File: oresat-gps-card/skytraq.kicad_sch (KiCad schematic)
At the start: 12 parts, among them U23 ORION-B16

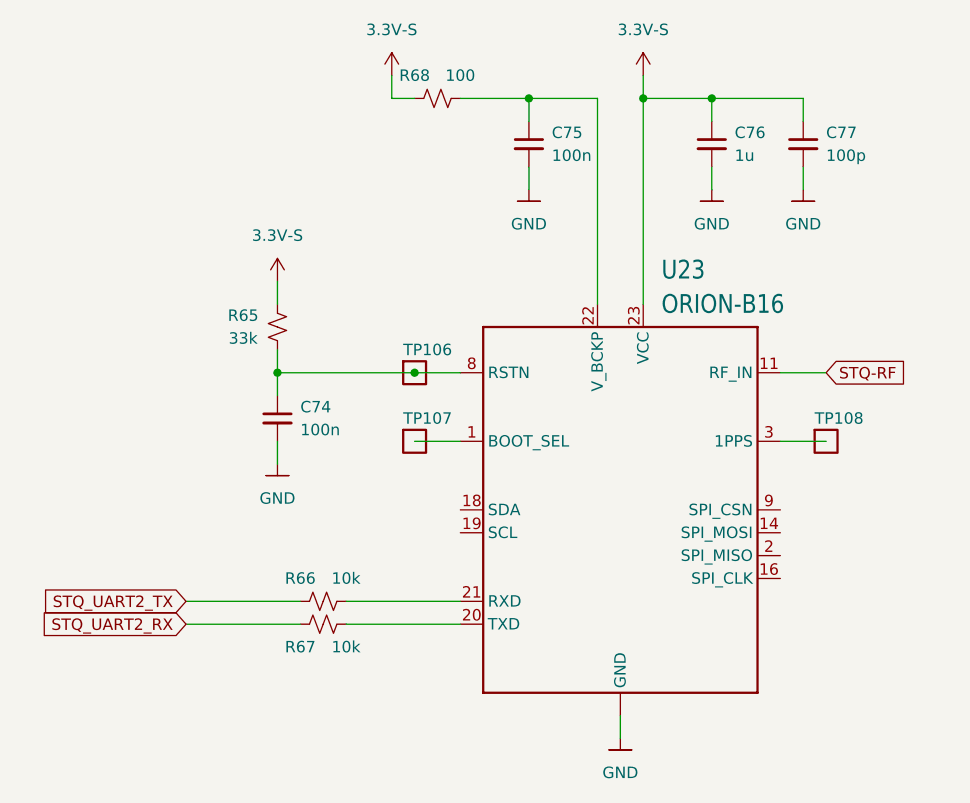
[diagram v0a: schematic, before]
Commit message: GPS card design review changes and issue fixes
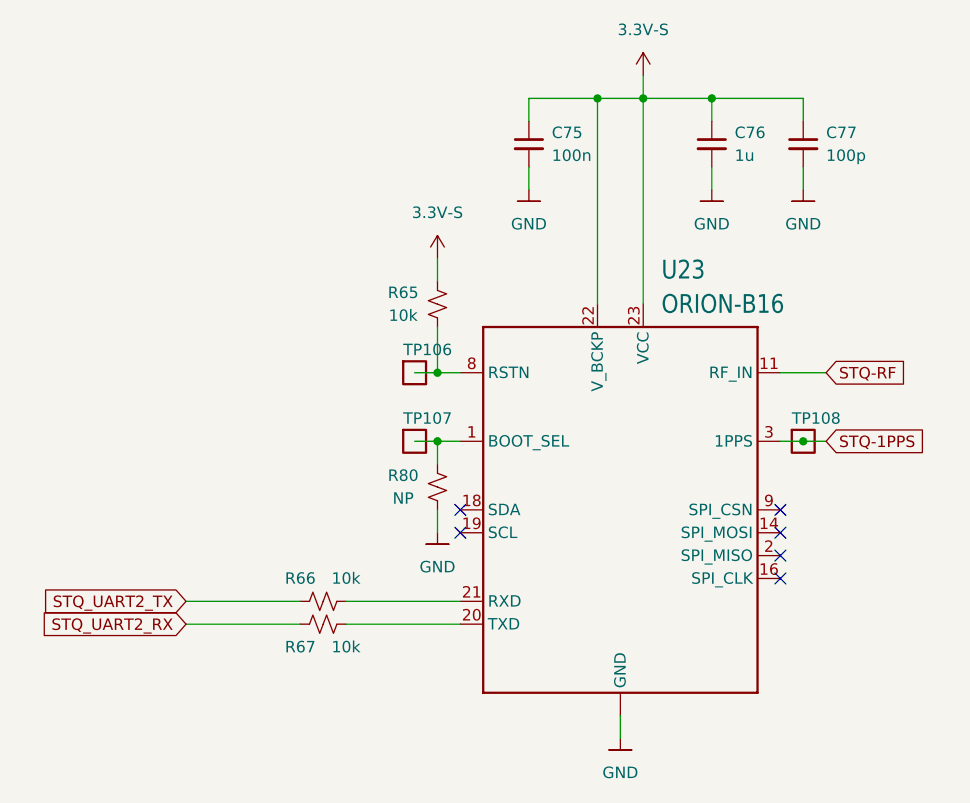
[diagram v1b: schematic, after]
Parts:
- removed C74: 100n, Capacitor_SMD:C_0603_1608Metric, symbol Device:C_Small
- removed R68: 100, Resistor_SMD:R_0603_1608Metric, symbol Device:R_Small_US
- added R80: NP, Resistor_SMD:R_0603_1608Metric, symbol Device:R_Small_US
- R65: value 33k -> 10k
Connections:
- net 3.3V-S: now also C75.1, U23.22 (V_BCKP)
- net GND: now also R80.2
- net at TP107.1, U23.1 (BOOT_SEL): now also R80.1
- net STQ-1PPS: now reaches TP108.1, U23.3 (1PPS)
- no-connect marks 0 -> 6
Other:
- moved on the sheet: TP108
